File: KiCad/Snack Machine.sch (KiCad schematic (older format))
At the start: 148 parts, among them J1 Screw_Terminal_01x02, J10 MDB, J11 Display Serial Header, J12 Conn_02x05_Odd_Even, J13 Conn_02x05_Odd_Even, J18 Conn_02x15_Counter_Clockwise, J2 AVR-ISP-6, J3 Screw_Terminal_01x08, J4 Screw_Terminal_01x08, J5 Conn_01x05_Female, J6 Screw_Terminal_01x02, J7 Conn_01x03_Female, J8 RFID_CONNECTOR, J9 MDB, Q1 P-CH 30V 3.8A, SW1 SW_SPST, U1 MEZD71202A-G, U2 MEZD71201A-F, U3 ATmega2560-16AU, Y1 16MHz

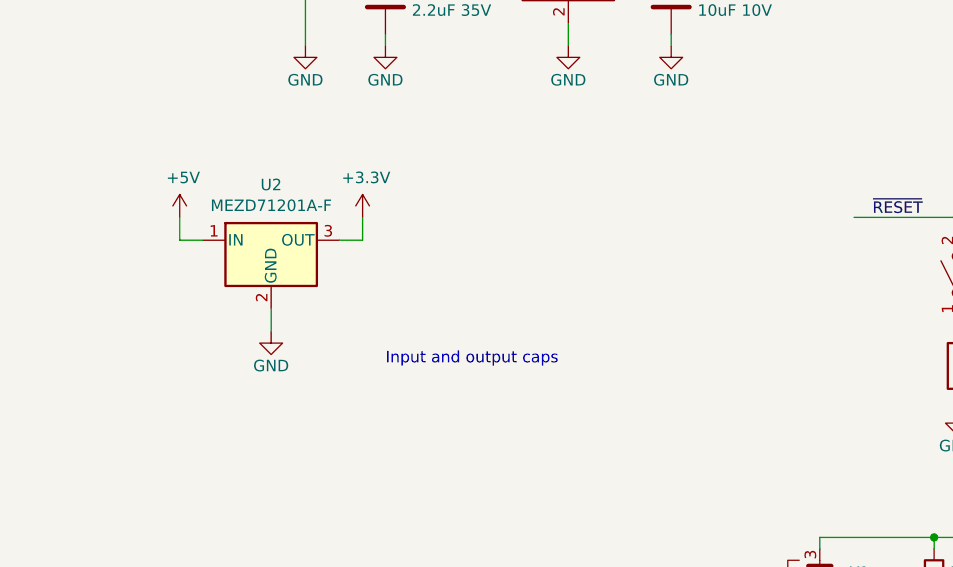
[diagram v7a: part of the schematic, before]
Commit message: Added input and output caps to 3.3V regulator
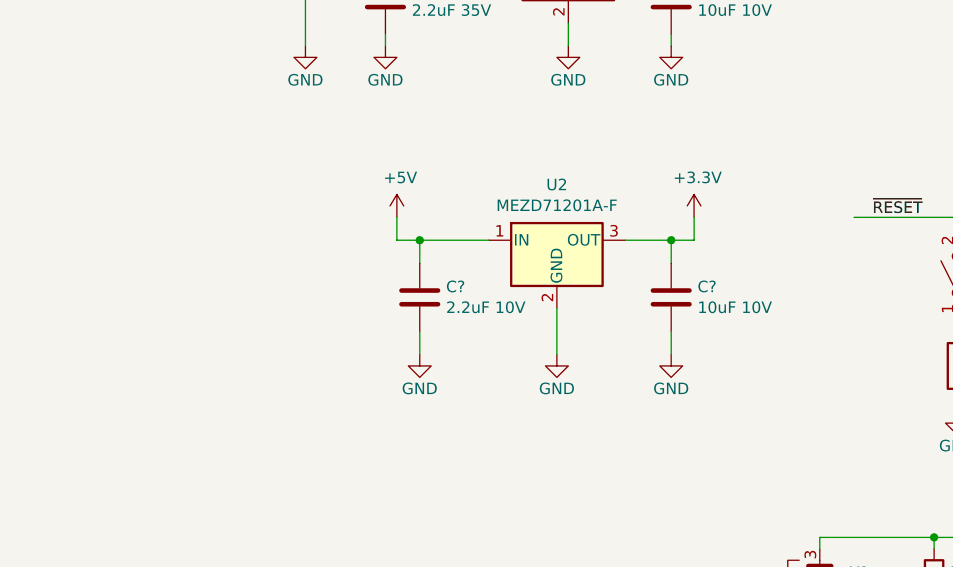
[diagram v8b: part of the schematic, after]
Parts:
- added C?: 2.2uF 10V, Capacitors_SMD:C_0805_HandSoldering, symbol Device:C
- added C?: 10uF 10V, Capacitors_SMD:C_0603_HandSoldering, symbol Device:C
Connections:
- wire segments 377 -> 383
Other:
- note removed: "Input and output caps"
- moved on the sheet: U2
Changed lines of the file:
@@
 L power:+5V #PWR?
 U 1 1 5BFF8049
-P 1800 2400
+P 2750 2400
 AR Path="/5BCD883C/5BFF8049" Ref="#PWR?"  Part="1"
 AR Path="/5BFF8049" Ref="#PWR023"  Part="1"
-F 0 "#PWR023" H 1800 2250 50  0001 C CNN
-F 1 "+5V" H 1815 2573 50  0000 C CNN
-F 2 "" H 1800 2400 50  0001 C CNN
-F 3 "" H 1800 2400 50  0001 C CNN
-	1    1800 2400
+F 0 "#PWR023" H 2750 2250 50  0001 C CNN
+F 1 "+5V" H 2765 2573 50  0000 C CNN
+F 2 "" H 2750 2400 50  0001 C CNN
+F 3 "" H 2750 2400 50  0001 C CNN
+	1    2750 2400
 	1    0    0    -1
 $EndComp
@@
 L Regulator_Linear:uA7805 U2
 U 1 1 5C00B376
-P 2200 2500
-F 0 "U2" H 2200 2742 50  0000 C CNN
-F 1 "MEZD71201A-F" H 2200 2651 50  0000 C CNN
-F 2 "" H 2225 2350 50  0001 L CIN
-F 3 "~" H 2200 2450 50  0001 C CNN
-	1    2200 2500
+P 3450 2500
+F 0 "U2" H 3450 2742 50  0000 C CNN
+F 1 "MEZD71201A-F" H 3450 2651 50  0000 C CNN
+F 2 "" H 3475 2350 50  0001 L CIN
+F 3 "~" H 3450 2450 50  0001 C CNN
+	1    3450 2500
 	1    0    0    -1
 $EndComp
@@
 L power:GND #PWR027
 U 1 1 5C00B441
-P 2200 2900
-F 0 "#PWR027" H 2200 2650 50  0001 C CNN
-F 1 "GND" H 2200 2750 50  0000 C CNN
-F 2 "" H 2200 2900 50  0001 C CNN
-F 3 "" H 2200 2900 50  0001 C CNN
-	1    2200 2900
-	1    0    0    -1
-$EndComp
-Wire Wire Line
-	2200 2800 2200 2900
-Wire Wire Line
-	1800 2400 1800 2500
-Wire Wire Line
-	1800 2500 1900 2500
+P 3450 3000
+F 0 "#PWR027" H 3450 2750 50  0001 C CNN
+F 1 "GND" H 3450 2850 50  0000 C CNN
+F 2 "" H 3450 3000 50  0001 C CNN
+F 3 "" H 3450 3000 50  0001 C CNN
+	1    3450 3000
+	1    0    0    -1
+$EndComp
+Wire Wire Line
+	3450 2800 3450 3000
 $Comp
 L power:+3.3V #PWR024
 U 1 1 5C031076
-P 2600 2400
-F 0 "#PWR024" H 2600 2250 50  0001 C CNN
-F 1 "+3.3V" H 2615 2573 50  0000 C CNN
-F 2 "" H 2600 2400 50  0001 C CNN
-F 3 "" H 2600 2400 50  0001 C CNN
-	1    2600 2400
-	1    0    0    -1
-$EndComp
-Wire Wire Line
-	2500 2500 2600 2500
-Wire Wire Line
-	2600 2500 2600 2400
+P 4050 2400
+F 0 "#PWR024" H 4050 2250 50  0001 C CNN
+F 1 "+3.3V" H 4065 2573 50  0000 C CNN
+F 2 "" H 4050 2400 50  0001 C CNN
+F 3 "" H 4050 2400 50  0001 C CNN
+	1    4050 2400
+	1    0    0    -1
+$EndComp
 Wire Wire Line
 	12400 4900 13350 4900
@@
 Wire Wire Line
 	9300 3100 9100 3100
-Text Notes 2700 3050 0    50   ~ 0
-Input and output caps
 $Comp
 L Connector_Generic:Conn_02x15_Counter_Clockwise J18
@@
 Wire Wire Line
 	1200 5500 900  5500
+$Comp
+L Device:C C?
+U 1 1 5C02D80D
+P 2850 2750
+F 0 "C?" H 2965 2796 50  0000 L CNN
+F 1 "2.2uF 10V" H 2965 2705 50  0000 L CNN
+F 2 "Capacitors_SMD:C_0805_HandSoldering" H 2888 2600 50  0001 C CNN
+F 3 "~" H 2850 2750 50  0001 C CNN
+F 4 "Samsung Electro-Mechanics" H 2850 2750 50  0001 C CNN "Manufacturer"
+F 5 "CL21B225KPFNNNE" H 2850 2750 50  0001 C CNN "Part Number"
+	1    2850 2750
+	1    0    0    -1
+$EndComp
+$Comp
+L Device:C C?
+U 1 1 5C02D96D
+P 3950 2750
+F 0 "C?" H 4065 2796 50  0000 L CNN
+F 1 "10uF 10V" H 4065 2705 50  0000 L CNN
+F 2 "Capacitors_SMD:C_0603_HandSoldering" H 3988 2600 50  0001 C CNN
+F 3 "~" H 3950 2750 50  0001 C CNN
+F 4 "AVX" H 3950 2750 50  0001 C CNN "Manufacturer"
+F 5 "0603ZD106KAT2A" H 3950 2750 50  0001 C CNN "Part Number"
+	1    3950 2750
+	1    0    0    -1
+$EndComp
+$Comp
+L power:GND #PWR?
+U 1 1 5C088194
+P 2850 3000
+F 0 "#PWR?" H 2850 2750 50  0001 C CNN
+F 1 "GND" H 2850 2850 50  0000 C CNN
+F 2 "" H 2850 3000 50  0001 C CNN
+F 3 "" H 2850 3000 50  0001 C CNN
+	1    2850 3000
+	1    0    0    -1
+$EndComp
+$Comp
+L power:GND #PWR?
+U 1 1 5C088497
+P 3950 3000
+F 0 "#PWR?" H 3950 2750 50  0001 C CNN
+F 1 "GND" H 3950 2850 50  0000 C CNN
+F 2 "" H 3950 3000 50  0001 C CNN
+F 3 "" H 3950 3000 50  0001 C CNN
+	1    3950 3000
+	1    0    0    -1
+$EndComp
+Wire Wire Line
+	2750 2400 2750 2500
+Wire Wire Line
+	2750 2500 2850 2500
+Wire Wire Line
+	2850 2600 2850 2500
+Connection ~ 2850 2500
+Wire Wire Line
+	2850 2500 3150 2500
+Wire Wire Line
+	2850 2900 2850 3000
+Wire Wire Line
+	4050 2500 4050 2400
+Wire Wire Line
+	3750 2500 3950 2500
+Wire Wire Line
+	3950 2500 3950 2600
+Connection ~ 3950 2500
+Wire Wire Line
+	3950 2500 4050 2500
+Wire Wire Line
+	3950 2900 3950 3000
 $EndSCHEMATC
